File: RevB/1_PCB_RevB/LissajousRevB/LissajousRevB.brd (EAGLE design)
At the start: 57.1 x 66 mm, 36 parts, among them U1 LM348D

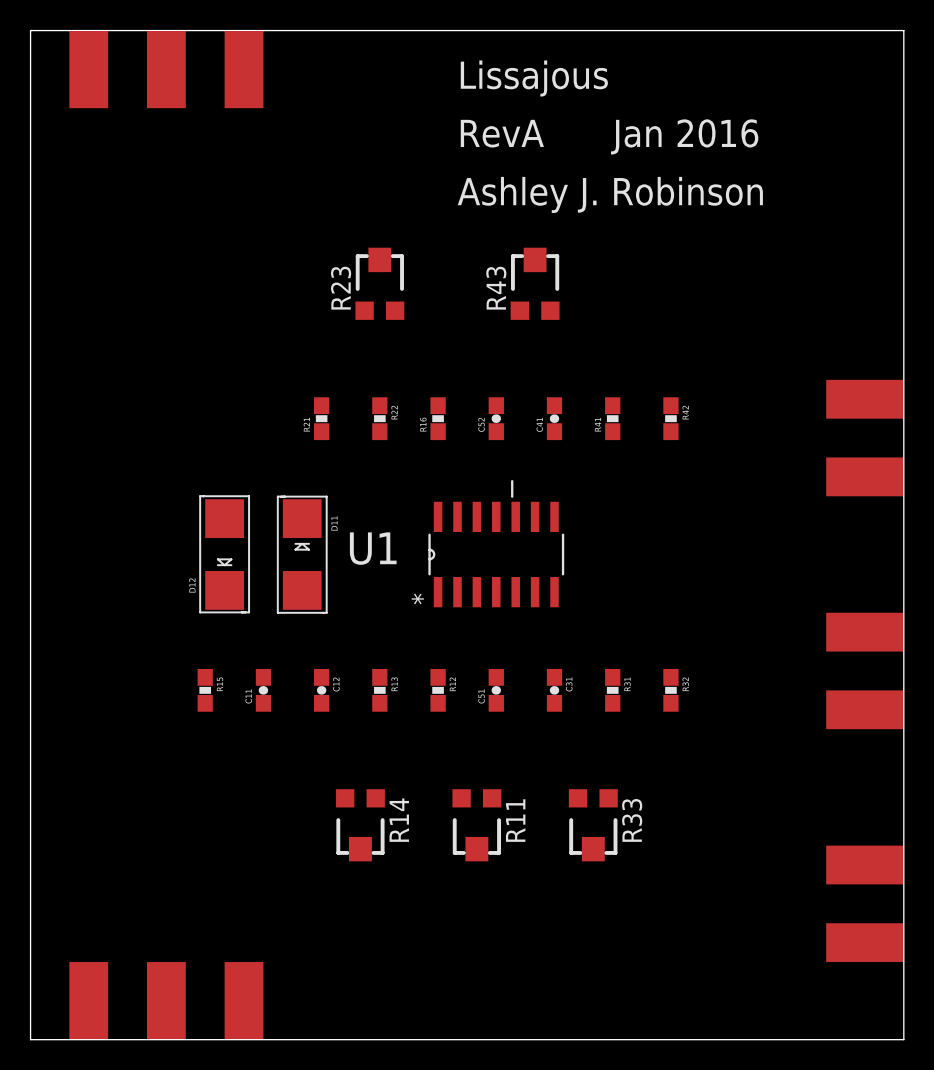
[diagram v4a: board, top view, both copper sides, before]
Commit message: first pass at routing
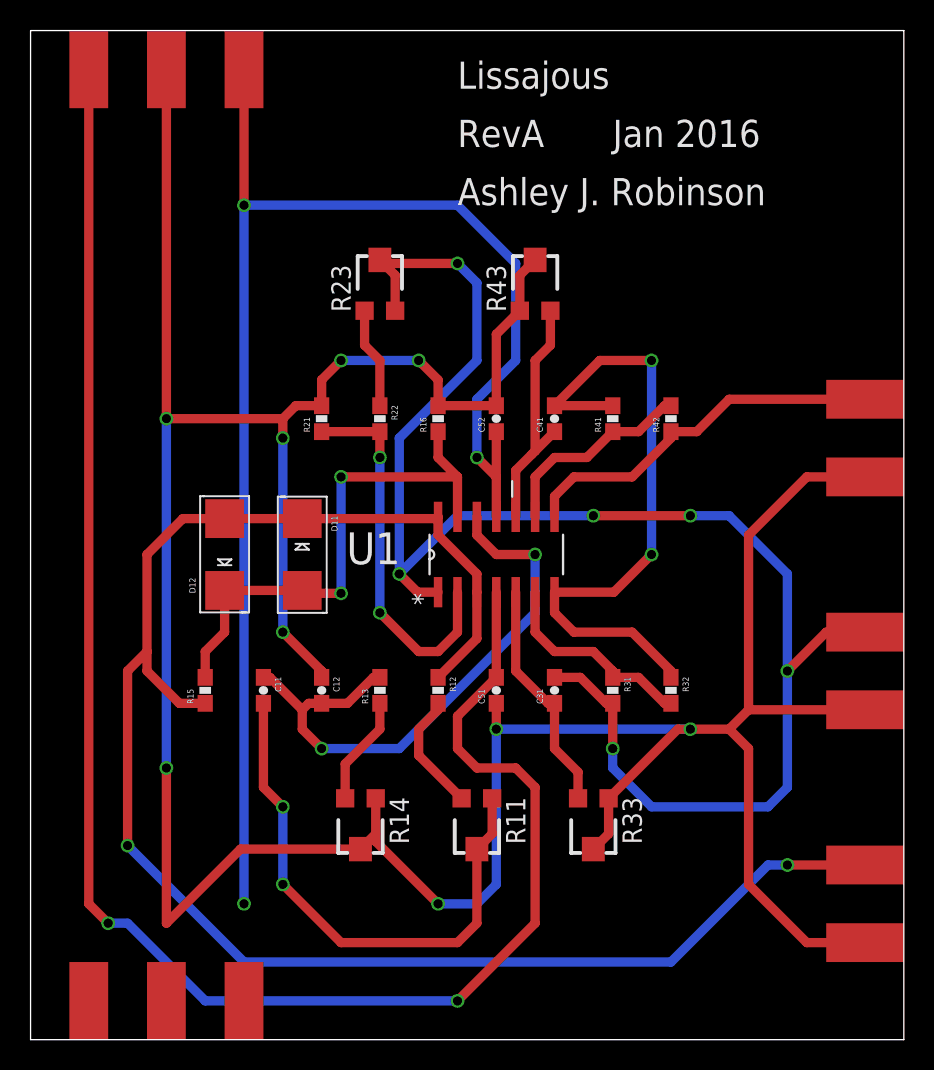
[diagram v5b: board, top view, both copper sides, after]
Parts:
- turned C11 to 270 degrees
- turned C31 to 90 degrees
- turned R13 to 90 degrees
- turned R15 to 90 degrees
- turned R42 to 90 degrees
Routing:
- net 0V: track 0.00 -> 229.1 mm, vias 0 -> 9
- net V+: track 0.00 -> 116.1 mm, vias 0 -> 2
- net SINE: track 0.00 -> 112.3 mm, vias 0 -> 2
- net N$12: track 0.00 -> 105.3 mm, vias 0 -> 6
- net V-: track 0.00 -> 95.1 mm, vias 0 -> 3
- net N$19: track 0.00 -> 42.4 mm, vias 0 -> 2
- net N$7: track 0.00 -> 39.4 mm, vias 0 -> 2
- net N$4: track 0.00 -> 35.8 mm, vias 0 -> 2
- net N$3: track 0.00 -> 35.3 mm, vias 0 -> 2
- net N$18: track 0.00 -> 25.8 mm
- net N$8: track 0.00 -> 24.9 mm, vias 0 -> 2
- net N$17: track 0.00 -> 16.2 mm
- net N$10: track 0.00 -> 15.4 mm
- net N$9: track 0.00 -> 13.7 mm
- net N$15: track 0.00 -> 13.4 mm
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
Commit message: ready to gen gerbers
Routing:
- net 0V: track 229.1 -> 256.6 mm
- net N$12: track 105.3 -> 89.1 mm, vias 6 -> 4
- net V+: track 116.1 -> 123.0 mm
- net SINE: track 112.3 -> 118.0 mm
- net V-: track 95.1 -> 99.3 mm
- net N$19: track 42.4 -> 46.0 mm
- net N$8: track 24.9 -> 23.1 mm
- net N$4: track 35.8 -> 35.0 mm, vias 2 -> 0
- added copper zone on layer 1, net 0V
- added copper zone on layer 16, net 0V
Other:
- board text added: "0V"
- board text added: "AMP"
- board text added: "OUT"
- board text added: "RevB"
- board text added: "SINE"
- board text added: "Sep 2016"
- board text added: "V+"
- board text added: "V-"
- board text removed: "Jan 2016"
- board text removed: "RevA"
